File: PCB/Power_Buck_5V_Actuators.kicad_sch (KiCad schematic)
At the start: 13 parts, among them J2 NID35-5

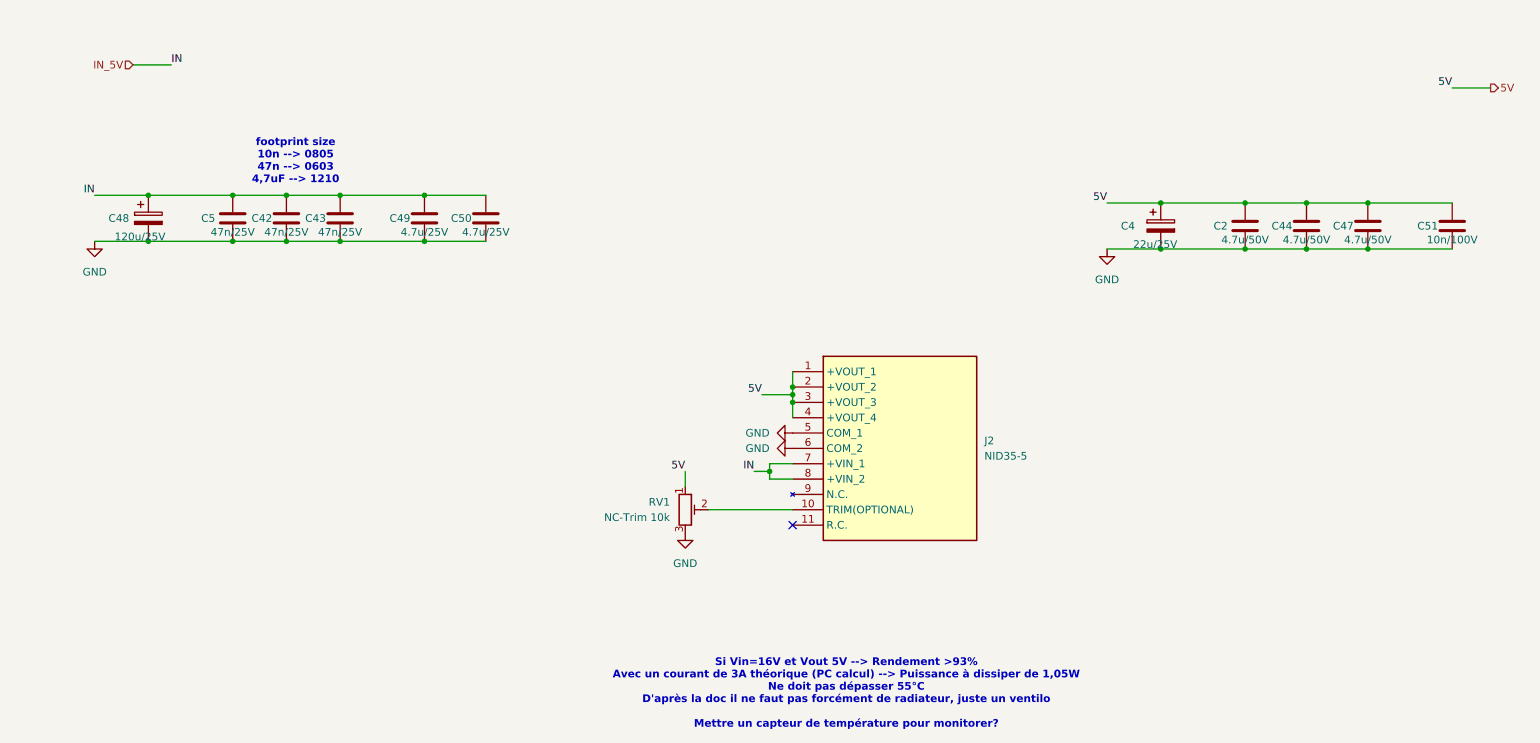
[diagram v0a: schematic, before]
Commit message: Updated a lot of stuff:
Added encoders,
Added 5V power supply for actuators
Added 12V power supply for actuators
Renamed sheets to be clearer
Added usb debug
Modify MCU sheet to be A3 format
Linked some pins
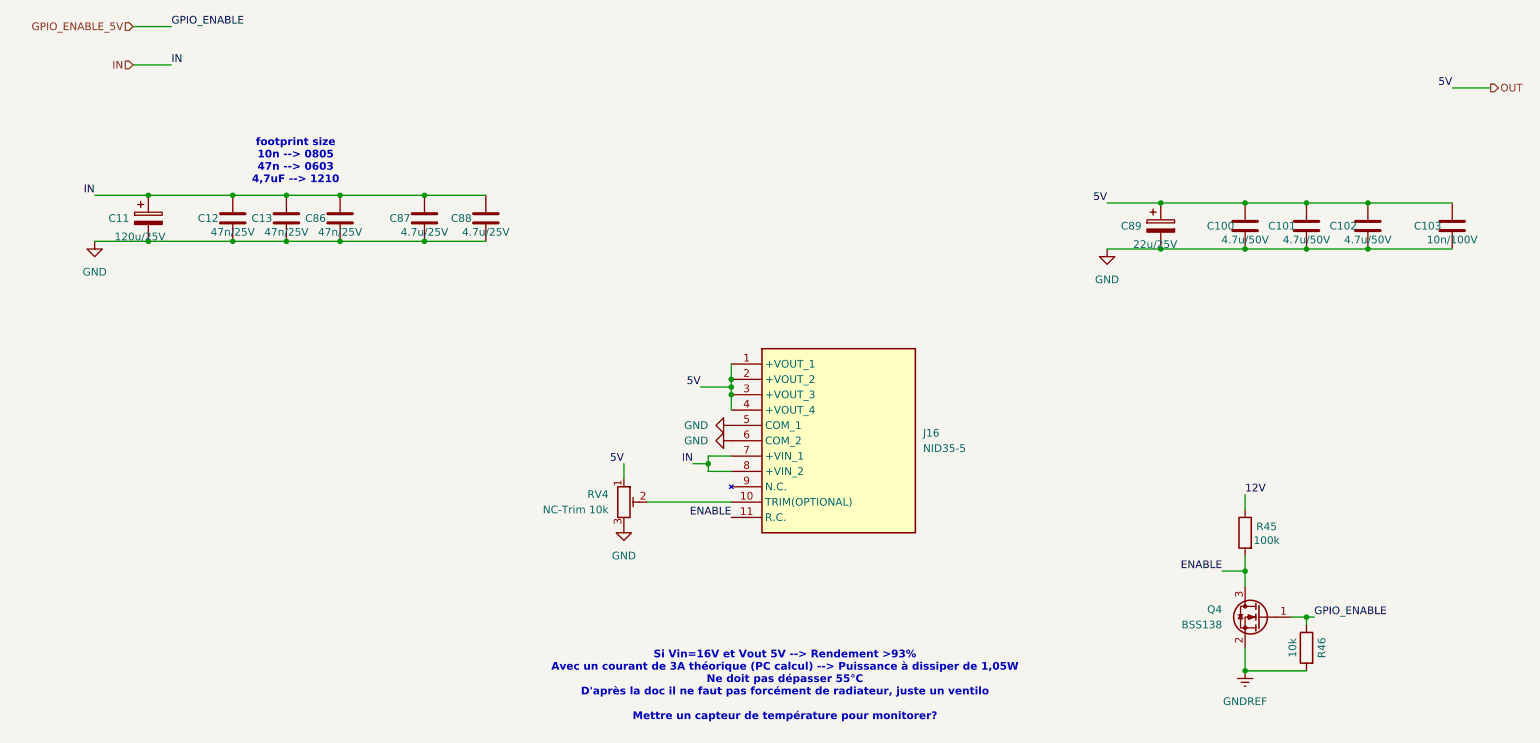
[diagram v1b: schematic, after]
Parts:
- added Q4: BSS138, Package_TO_SOT_SMD:SOT-23, symbol Transistor_FET:BSS138
- added R45: 100k, symbol Device:R
- added R46: 10k, symbol Device:R
- renumbered C2 to C100, C44 to C101, C47 to C102, C51 to C103, C48 to C11, C5 to C12, C42 to C13, C43 to C86, C49 to C87, C50 to C88, C4 to C89, J2 to J16, RV1 to RV4
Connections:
- net ENABLE: now reaches J16.11 (R.C.)
- net ENABLE: now also Q4.3 (D), R45.2
- net 5V renamed OUT
- net IN_5V renamed IN
- new net 12V: R45.1
- new net GNDREF: Q4.2 (S), R46.2
- new net GPIO_ENABLE_5V: Q4.1 (G), R46.1
- no-connect marks 1 -> 0
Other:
- moved on the sheet: J16, RV4
